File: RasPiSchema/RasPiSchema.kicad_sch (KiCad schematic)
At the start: 6 parts, among them J1 GPIO, U1 CAT24C256

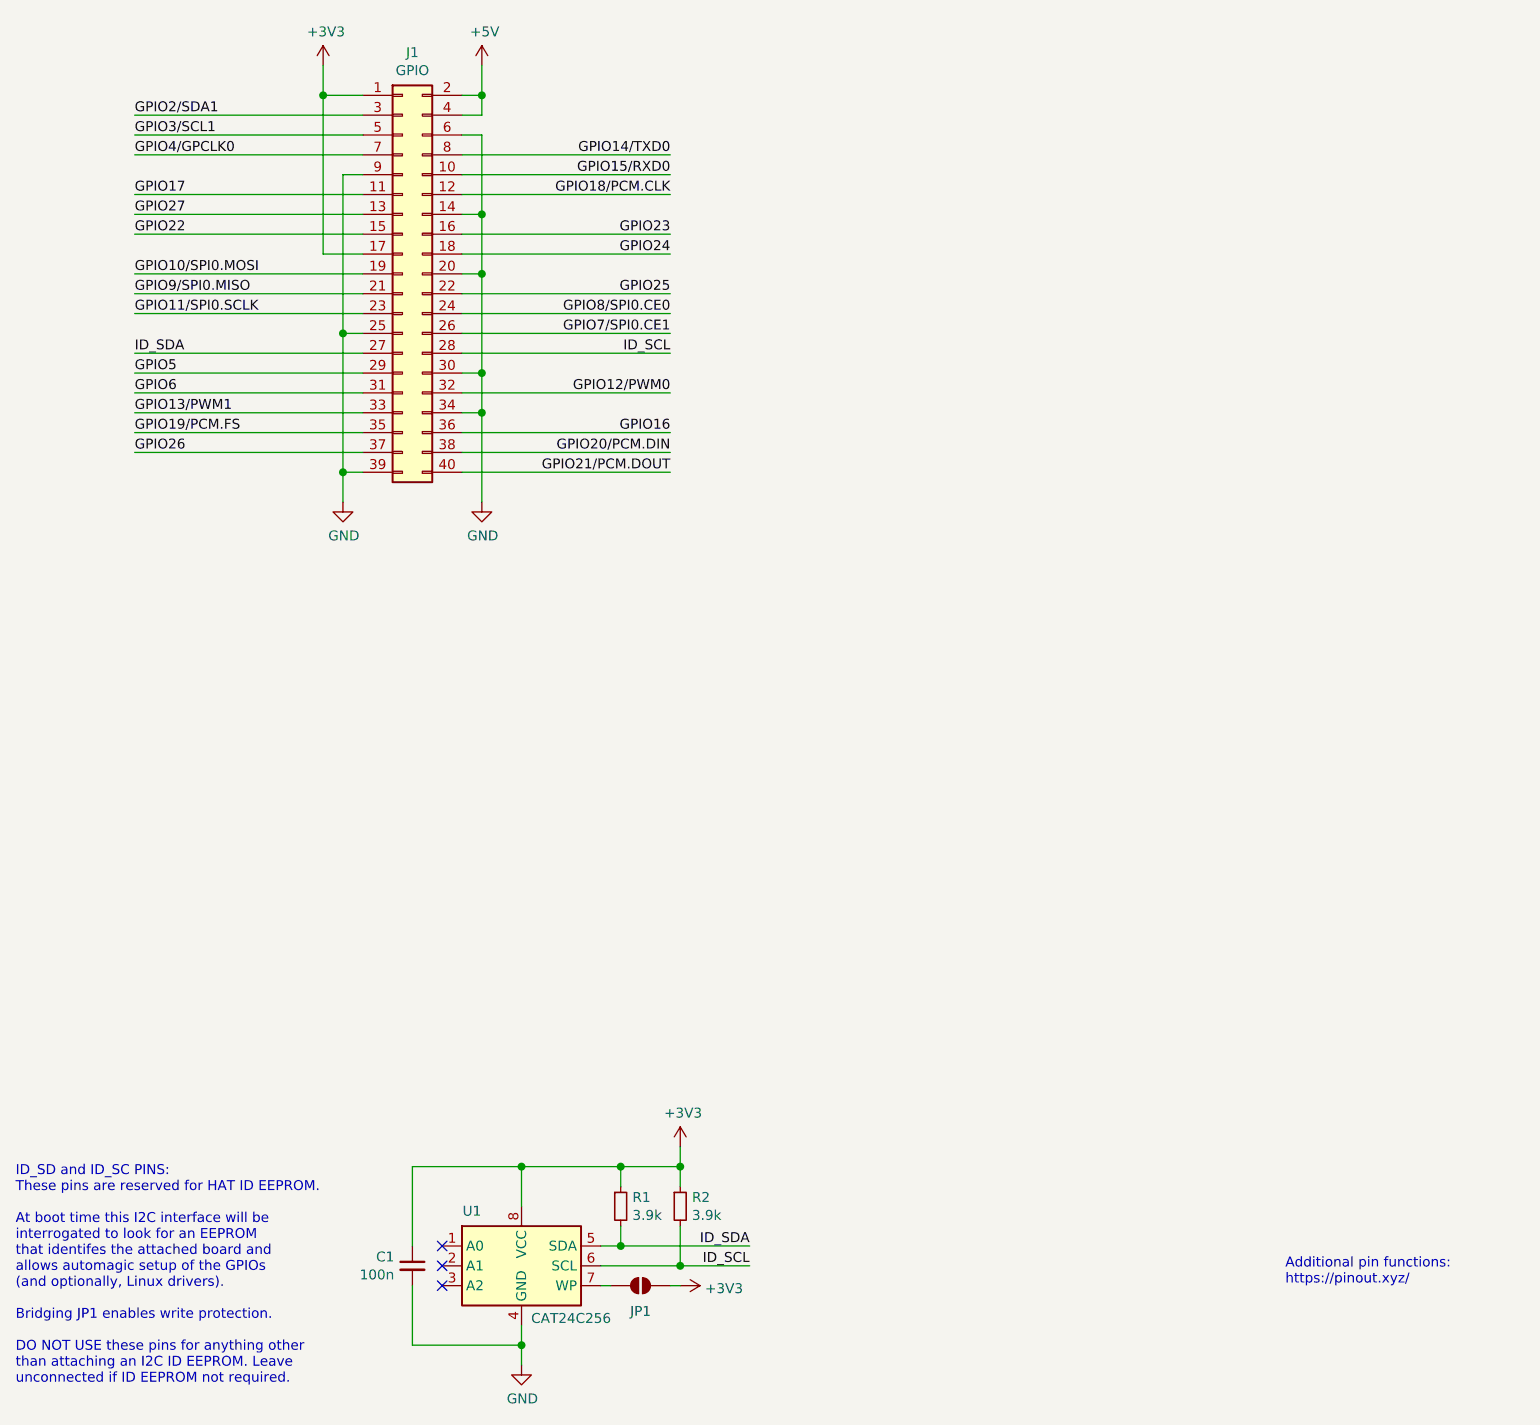
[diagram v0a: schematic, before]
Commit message: Add Raspberry Pi camera and Raspberry Pi CSI connector schematics
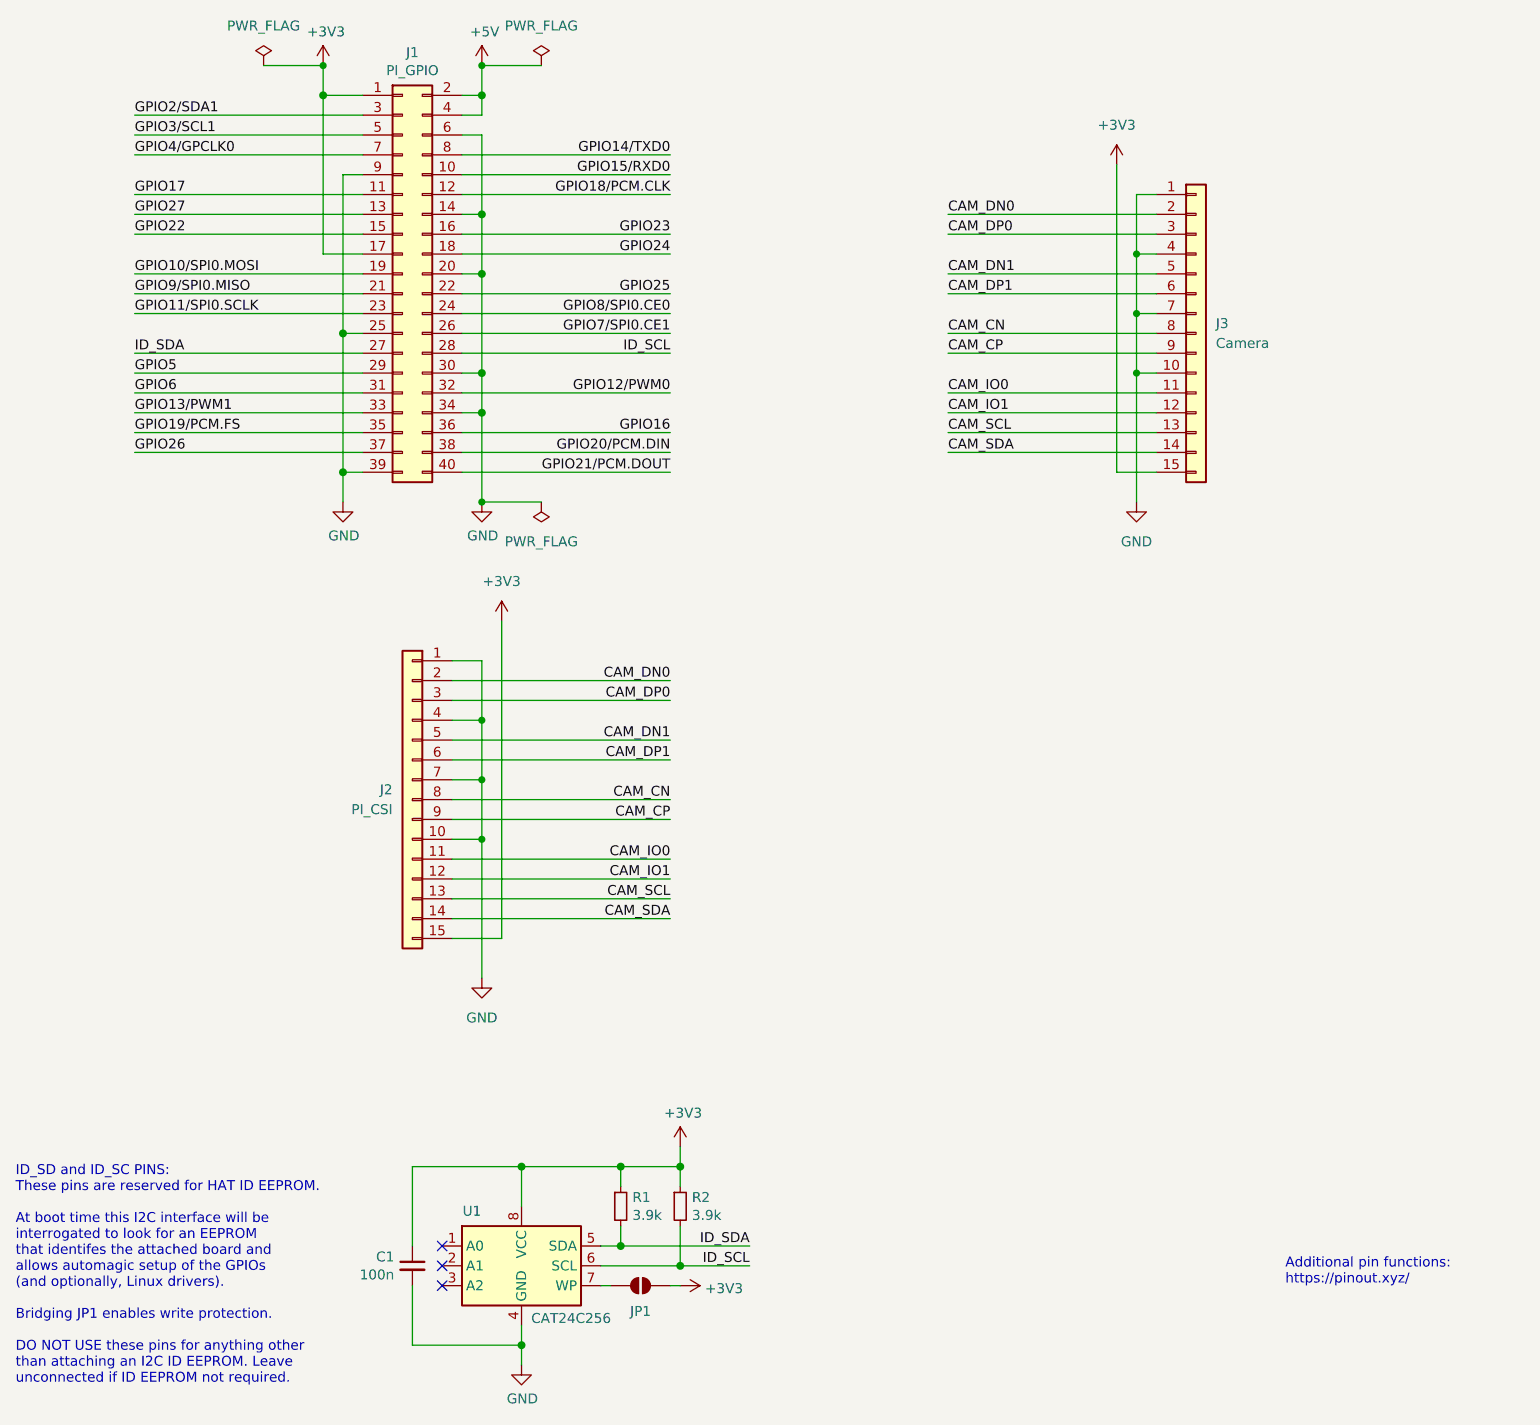
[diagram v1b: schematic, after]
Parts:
- added J2: PI_CSI, symbol Connector_Generic:Conn_01x15
- added J3: Camera, symbol Connector_Generic:Conn_01x15
- J1: value GPIO -> PI_GPIO
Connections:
- net +3V3: now also J2.15 (Pin_15), J3.15 (Pin_15)
- net GND: now also J2.1 (Pin_1), J2.10 (Pin_10), J2.4 (Pin_4), J2.7 (Pin_7), J3.1 (Pin_1), J3.10 (Pin_10), J3.4 (Pin_4), J3.7 (Pin_7)
- new net CAM_CN: J2.8 (Pin_8), J3.8 (Pin_8)
- new net CAM_CP: J2.9 (Pin_9), J3.9 (Pin_9)
- new net CAM_DN0: J2.2 (Pin_2), J3.2 (Pin_2)
- new net CAM_DN1: J2.5 (Pin_5), J3.5 (Pin_5)
- new net CAM_DP0: J2.3 (Pin_3), J3.3 (Pin_3)
- new net CAM_DP1: J2.6 (Pin_6), J3.6 (Pin_6)
- new net CAM_IO0: J2.11 (Pin_11), J3.11 (Pin_11)
- new net CAM_IO1: J2.12 (Pin_12), J3.12 (Pin_12)
- new net CAM_SCL: J2.13 (Pin_13), J3.13 (Pin_13)
- new net CAM_SDA: J2.14 (Pin_14), J3.14 (Pin_14)
